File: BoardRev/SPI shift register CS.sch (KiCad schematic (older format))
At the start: 19 parts, among them J1 CONN_06, J10 CONN_07, J2 CONN_06, J3 CONN_06, J4 CONN_06, J5 CONN_06, J6 CONN_06, J7 CONN_06, J8 CONN_06, J9 CONN_07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

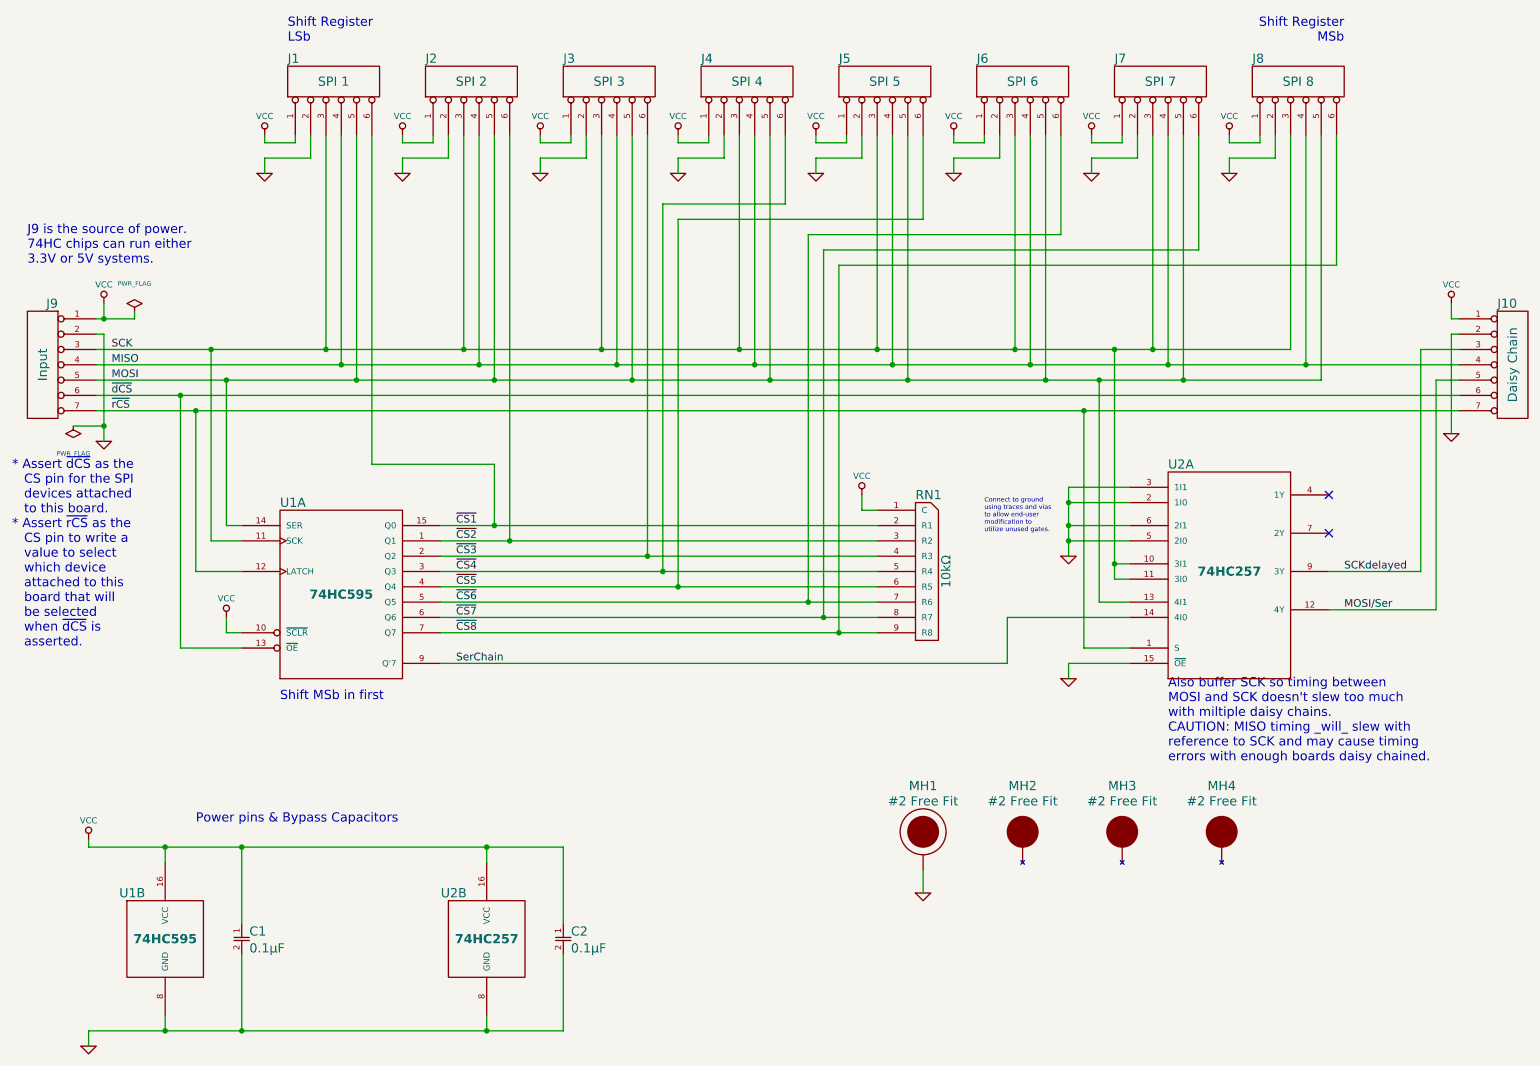
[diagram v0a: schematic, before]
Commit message: Initial 1" square SMT version
Signed-off-by: Chris 'Sembazuru' Elliott <SembazuruCDE@GMail.com>
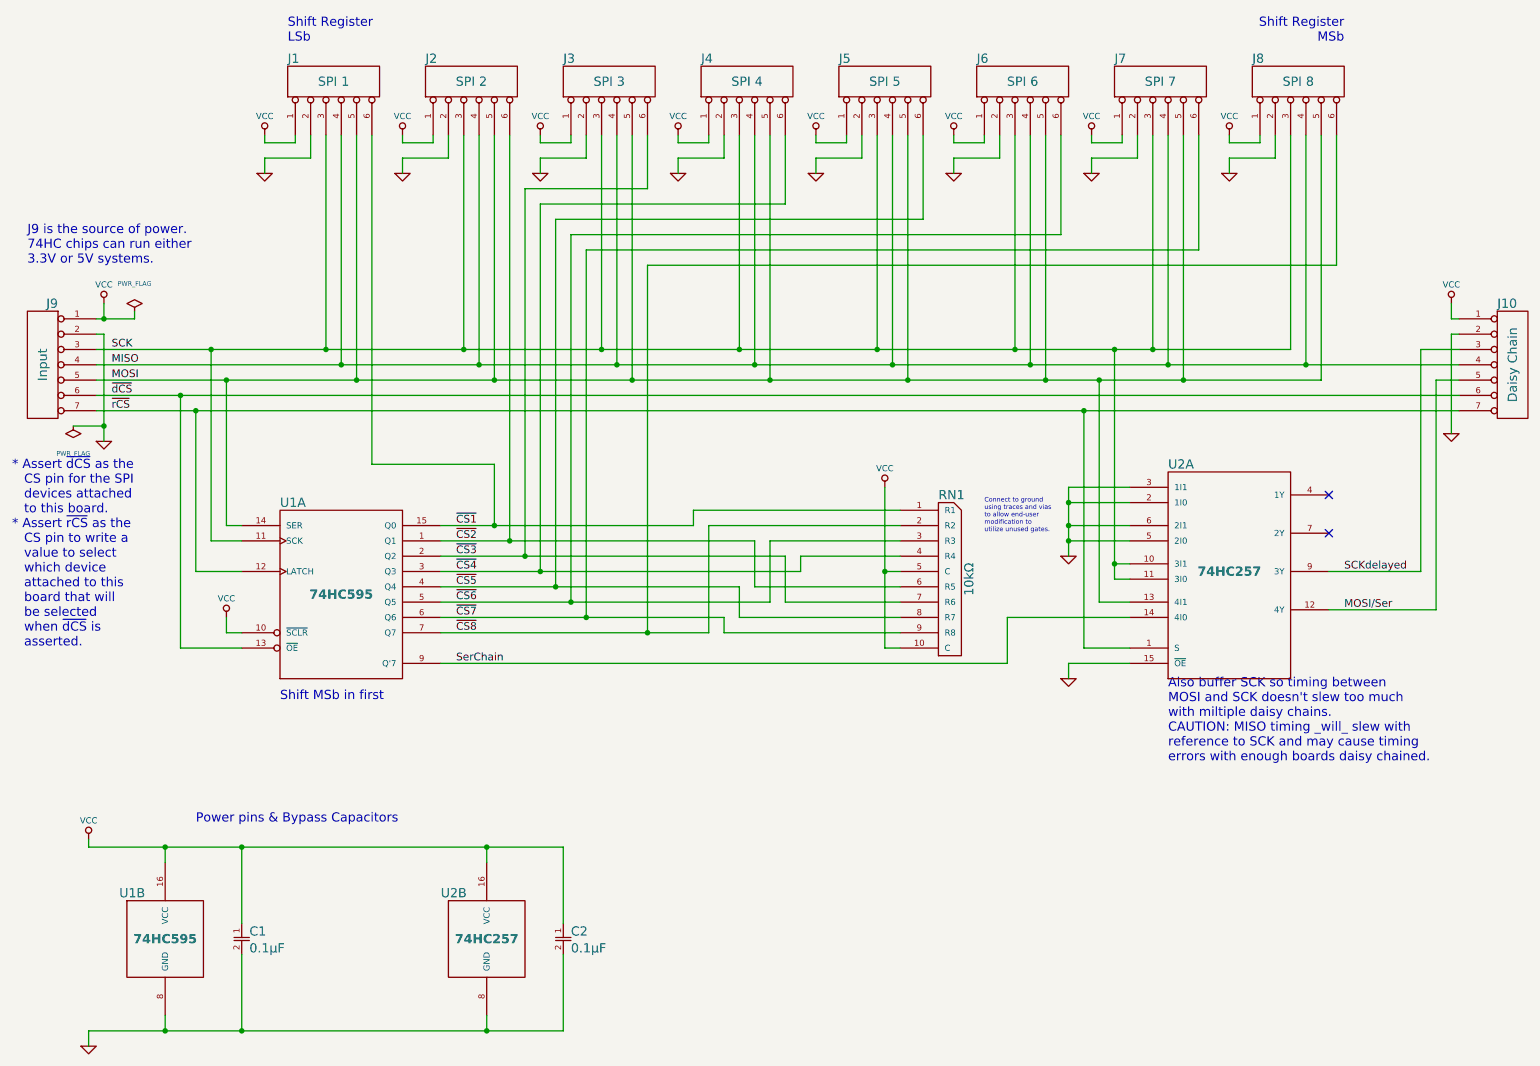
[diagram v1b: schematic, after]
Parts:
- removed MH1: #2 Free Fit, ipc-7251TH Standard:MTGP635H244V8P, symbol MOUNTING_HOLE_PTH
- removed MH2, MH3, MH4: #2 Free Fit, ipc-7251TH Standard:MTGNP635H244Z635P, symbol MOUNTING_HOLE_NPTH
- removed RN1: 10kΩ, ipc-7251TH Standard:SIP249W55P254L2261H495Q9C, symbol RN8BUSSIP
- added RN1: 10kΩ, CDE_misc:RESCAV_EXBA-10N, symbol RN8BUSDIP
- C1, C2: footprint ipc-7251TH Standard:CAPRR254W51L508T318H660P -> AVX-06035C104KAT2A:CAPC1608X90N; CommonPartLibrary (none) -> CPL-CAP-X7R-0603-100NF-50V; Mfg (none) -> AVX; Mfg2 (none) -> Kemet; Mfg2Part (none) -> C0603C104K5RACTU; MfgPart (none) -> 06035C104KAT2A
- J1, J2, J3, J4, J5, J6, J7, J8: footprint ipc-7251TH Standard:HDRV6W64P254_1X6_1524X254X1016P -> ipc-7251TH-standard:HDRV6W64P254_1X6_1524X254X1016P
- U1: footprint ipc-7251TH Standard:DIP762W52P254L2159H381Q16C -> NXP-74HC595PW_118:SOP65P640X110-16N; CommonPartLibrary (none) -> CPL-; Mfg (none) -> Texas Instruments; MfgPart (none) -> SN74HC595PWR
- U2: footprint ipc-7251TH Standard:DIP762W52P254L2159H381Q16C -> TI-SN74HC257PW:SOP65P640X120-16N; CommonPartLibrary (none) -> CPL-; Mfg (none) -> Texas Instruments; MfgPart (none) -> SN74HC257PW
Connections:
- net VCC: now also RN1.10 (C), RN1.5 (C)
- net ~CS1: now also RN1.1 (R1)
- net ~CS2: now also RN1.6 (R5)
- net ~CS3: now also RN1.7 (R6)
- net ~CS4: now also RN1.4 (R4)
- net ~CS5: now also RN1.8 (R7)
- net ~CS6: now also RN1.3 (R3)
- net ~CS7: now also RN1.9 (R8)
- net ~CS8: now also RN1.2 (R2)

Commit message: collected updates
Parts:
- C1, C2: Characteristics (none) -> CAP CER 0.1UF 50V 5% X7R 0603; Critical (none) -> N; Description (none) -> Capacitor - Bypass; MFN (none) -> AVX; MFP (none) -> 06035C104KAT2A; Mfg AVX -> (none); Mfg2 Kemet -> (none); Mfg2Part C0603C104K5RACTU -> (none); MfgPart 06035C104KAT2A -> (none); Notes (none) -> 15WVDC or better, 10% tolerance or better.; Package ID (none) -> 0603 [1608 Metric]; S1PL (none) -> http://www.digikey.com/product-detail/en/06035C104KAT2A/478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; S1PN (none) -> 478-5052-1-ND; S2PL (none) -> http://www.newark.com/avx/06035c104kat2a/ceramic-capacitor-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; S2PN (none) -> 54K2412; Source (none) -> ANY
- J10: Characteristics (none) -> Voltage / Current / Tolerance / Ect specs; CommonPartLibrary (none) -> CPL-; Critical (none) -> Y / N; Description (none) -> Pin header - Daisy chain output to next board.; MFN (none) -> Manufacturer Name; MFP (none) -> Manufacturer Part Number; Notes (none) -> Explain critera for \"ANY\" Source; Package ID (none) -> JEDEC footprint name; S1PL (none) -> Source1 Product Link; S1PN (none) -> Source1 Part Number; S2PL (none) -> Source2 Product Link; S2PN (none) -> Source2 Part Number; Source (none) -> ANY / SPEC
- J9: Characteristics (none) -> Voltage / Current / Tolerance / Ect specs; CommonPartLibrary (none) -> CPL-; Critical (none) -> N; Description (none) -> Pin header - Board input; MFN (none) -> Manufacturer Name; MFP (none) -> Manufacturer Part Number; Notes (none) -> Designed for 0.1\" spacing, 0.25\"sq pins.; Package ID (none) -> JEDEC footprint name; S1PL (none) -> Source1 Product Link; S1PN (none) -> Source1 Part Number; S2PL (none) -> Source2 Product Link; S2PN (none) -> Source2 Part Number; Source (none) -> ANY
- RN1: MFN (none) -> Panasonic; MFP (none) -> EXB-A10P103J; Mfg Panasonic -> (none); MfgPart EXB-A10P103J -> (none)
- U1: MFN (none) -> Texas Instruments; MFP (none) -> SN74HC595PWR; Mfg Texas Instruments -> (none); MfgPart SN74HC595PWR -> (none)
- U2: MFN (none) -> Texas Instruments; MFP (none) -> SN74HC257PW; Mfg Texas Instruments -> (none); MfgPart SN74HC257PW -> (none)
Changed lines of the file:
@@
 Sheet 1 1
 Title "SPI Shift Register 8 Device Select"
-Date "2016-02-25"
-Rev "2.0.0"
+Date "2016-04-16"
+Rev "2.0.1"
 Comp "Sembazuru Circuits"
 Comment1 "Intended to be released as OSHW"
 Comment2 "v1.0 - First iteration"
 Comment3 "v2.0.0 - Convert part numbers and footprints to SMT versions (except for headers)."
-Comment4 ""
+Comment4 "v2.0.1 - Add additional component fields in the spirit of RheingoldHeavy's BOM management"
 $EndDescr
 $Comp
@@
 F 2 "ipc-7251TH Standard:HDRV7W64P254_1X7_1778X254X1016P" H 10300 3150 60  0001 C CNN
 F 3 "" H 10300 3150 60  0000 C CNN
-F 4 "Daisy Chain" V 10300 3150 60  0000 C CNN "Note"
+F 4 "CPL-" H 10300 3150 60  0001 C CNN "CommonPartLibrary"
+F 5 "Manufacturer Name" H 10300 3150 60  0001 C CNN "MFN"
+F 6 "Manufacturer Part Number" H 10300 3150 60  0001 C CNN "MFP"
+F 7 "JEDEC footprint name" H 10300 3150 60  0001 C CNN "Package ID"
+F 8 "Source1 Part Number" H 10300 3150 60  0001 C CNN "S1PN"
+F 9 "Source1 Product Link" H 10300 3150 60  0001 C CNN "S1PL"
+F 10 "Source2 Part Number" H 10300 3150 60  0001 C CNN "S2PN"
+F 11 "Source2 Product Link" H 10300 3150 60  0001 C CNN "S2PL"
+F 12 "Voltage / Current / Tolerance / Ect specs" H 10300 3150 60  0001 C CNN "Characteristics"
+F 13 "Pin header - Daisy chain output to next board." H 10300 3150 60  0001 C CNN "Description"
+F 14 "Y / N" H 10300 3150 60  0001 C CNN "Critical"
+F 15 "ANY / SPEC" H 10300 3150 60  0001 C CNN "Source"
+F 16 "Explain critera for \"ANY\" Source" H 10300 3150 60  0001 C CNN "Notes"
+F 17 "Daisy Chain" V 10300 3150 60  0000 C CNN "Note"
 	1    10300 3150
 	1    0    0    -1
@@
 F 2 "ipc-7251TH Standard:HDRV7W64P254_1X7_1778X254X1016P" H 700 3150 60  0001 C CNN
 F 3 "" H 700 3150 60  0000 C CNN
-F 4 "Input" V 700 3150 60  0000 C CNN "Note"
+F 4 "CPL-" H 700 3150 60  0001 C CNN "CommonPartLibrary"
+F 5 "Manufacturer Name" H 700 3150 60  0001 C CNN "MFN"
+F 6 "Manufacturer Part Number" H 700 3150 60  0001 C CNN "MFP"
+F 7 "JEDEC footprint name" H 700 3150 60  0001 C CNN "Package ID"
+F 8 "Source1 Part Number" H 700 3150 60  0001 C CNN "S1PN"
+F 9 "Source1 Product Link" H 700 3150 60  0001 C CNN "S1PL"
+F 10 "Source2 Part Number" H 700 3150 60  0001 C CNN "S2PN"
+F 11 "Source2 Product Link" H 700 3150 60  0001 C CNN "S2PL"
+F 12 "Voltage / Current / Tolerance / Ect specs" H 700 3150 60  0001 C CNN "Characteristics"
+F 13 "Pin header - Board input" H 700 3150 60  0001 C CNN "Description"
+F 14 "N" H 700 3150 60  0001 C CNN "Critical"
+F 15 "ANY" H 700 3150 60  0001 C CNN "Source"
+F 16 "Designed for 0.1\" spacing, 0.25\"sq pins." H 700 3150 60  0001 C CNN "Notes"
+F 17 "Input" V 700 3150 60  0000 C CNN "Note"
 	1    700  3150
 	-1   0    0    -1
@@
 F 3 "https://octopart.com/sn74hc595pwr-texas+instruments-879136" H 2650 4650 60  0001 C CNN
 F 4 "CPL-" H 2650 4650 60  0001 C CNN "CommonPartLibrary"
-F 5 "Texas Instruments" H 2650 4650 60  0001 C CNN "Mfg"
-F 6 "SN74HC595PWR" H 2650 4650 60  0001 C CNN "MfgPart"
+F 5 "Texas Instruments" H 2650 4650 60  0001 C CNN "MFN"
+F 6 "SN74HC595PWR" H 2650 4650 60  0001 C CNN "MFP"
 	1    2650 4650
 	1    0    0    -1
@@
 F 3 "https://octopart.com/sn74hc257pw-texas+instruments-789437" H 8450 4600 60  0001 C CNN
 F 4 "CPL-" H 8450 4500 60  0001 C CNN "CommonPartLibrary"
-F 5 "Texas Instruments" H 8450 4500 60  0001 C CNN "Mfg"
-F 6 "SN74HC257PW" H 8450 4500 60  0001 C CNN "MfgPart"
+F 5 "Texas Instruments" H 8450 4500 60  0001 C CNN "MFN"
+F 6 "SN74HC257PW" H 8450 4500 60  0001 C CNN "MFP"
 	1    8450 4500
 	1    0    0    -1
@@
 F 3 "https://octopart.com/common-parts-library#CPL-CAP-X7R-0603-100NF-50V" H 2000 6900 60  0001 C CNN
 F 4 "CPL-CAP-X7R-0603-100NF-50V" H 2000 6900 60  0001 C CNN "CommonPartLibrary"
-F 5 "AVX" H 2000 6900 60  0001 C CNN "Mfg"
-F 6 "06035C104KAT2A" H 2000 6900 60  0001 C CNN "MfgPart"
-F 7 "Kemet" H 2000 6900 60  0001 C CNN "Mfg2"
-F 8 "C0603C104K5RACTU" H 2000 6900 60  0001 C CNN "Mfg2Part"
+F 5 "AVX" H 2000 6900 60  0001 C CNN "MFN"
+F 6 "06035C104KAT2A" H 2000 6900 60  0001 C CNN "MFP"
+F 7 "0603 [1608 Metric]" H 2000 6900 60  0001 C CNN "Package ID"
+F 8 "478-5052-1-ND" H 2000 6900 60  0001 C CNN "S1PN"
+F 9 "http://www.digikey.com/product-detail/en/06035C104KAT2A/478-5052-1-ND/" H 2000 6900 60  0001 C CNN "S1PL"
+F 10 "54K2412" H 2000 6900 60  0001 C CNN "S2PN"
+F 11 "http://www.newark.com/avx/06035c104kat2a/ceramic-capacitor-0-1uf-50v-x7r/dp/54K2412" H 2000 6900 60  0001 C CNN "S2PL"
+F 12 "CAP CER 0.1UF 50V 5% X7R 0603" H 2000 6900 60  0001 C CNN "Characteristics"
+F 13 "Capacitor - Bypass" H 2000 6900 60  0001 C CNN "Description"
+F 14 "N" H 2000 6900 60  0001 C CNN "Critical"
+F 15 "ANY" H 2000 6900 60  0001 C CNN "Source"
+F 16 "15WVDC or better, 10% tolerance or better." H 2000 6900 60  0001 C CNN "Notes"
 	1    2000 6900
 	1    0    0    -1
@@
 Connect to ground\nusing traces and vias\nto allow end-user\nmodification to\nutilize unused gates.
 $Comp
-L CAP_NP C2
-U 1 1 56CE7844
-P 4100 6900
-F 0 "C2" H 4150 6950 60  0000 L CNN
-F 1 "0.1µF" H 4150 6840 60  0000 L CNN
-F 2 "AVX-06035C104KAT2A:CAPC1608X90N" H 4100 6900 60  0001 C CNN
-F 3 "https://octopart.com/common-parts-library#CPL-CAP-X7R-0603-100NF-50V" H 4100 6900 60  0001 C CNN
-F 4 "CPL-CAP-X7R-0603-100NF-50V" H 4100 6900 60  0001 C CNN "CommonPartLibrary"
-F 5 "AVX" H 4100 6900 60  0001 C CNN "Mfg"
-F 6 "06035C104KAT2A" H 4100 6900 60  0001 C CNN "MfgPart"
-F 7 "Kemet" H 4100 6900 60  0001 C CNN "Mfg2"
-F 8 "C0603C104K5RACTU" H 4100 6900 60  0001 C CNN "Mfg2Part"
-	1    4100 6900
-	1    0    0    -1
-$EndComp
-$Comp
 L 74HC595 U1
 U 2 1 56CE85CE
@@
 F 3 "https://octopart.com/sn74hc595pwr-texas+instruments-879136" H 1500 6900 60  0001 C CNN
 F 4 "CPL-" H 1500 6900 60  0001 C CNN "CommonPartLibrary"
-F 5 "Texas Instruments" H 1500 6900 60  0001 C CNN "Mfg"
-F 6 "SN74HC595PWR" H 1500 6900 60  0001 C CNN "MfgPart"
+F 5 "Texas Instruments" H 1500 6900 60  0001 C CNN "MFN"
+F 6 "SN74HC595PWR" H 1500 6900 60  0001 C CNN "MFP"
 	2    1500 6900
 	1    0    0    -1
@@
 F 3 "https://octopart.com/sn74hc257pw-texas+instruments-789437" H 3600 7000 60  0001 C CNN
 F 4 "CPL-" H 3600 6900 60  0001 C CNN "CommonPartLibrary"
-F 5 "Texas Instruments" H 3600 6900 60  0001 C CNN "Mfg"
-F 6 "SN74HC257PW" H 3600 6900 60  0001 C CNN "MfgPart"
+F 5 "Texas Instruments" H 3600 6900 60  0001 C CNN "MFN"
+F 6 "SN74HC257PW" H 3600 6900 60  0001 C CNN "MFP"
 	2    3600 6900
 	1    0    0    -1
@@
 F 3 "https://octopart.com/exb-a10p103j-panasonic-42270834" H 6600 4600 60  0001 C CNN
 F 4 "CPL-ARRB-2512-10KOHM-0.062W*" H 6600 4550 30  0001 C CNN "CommonPartLibrary"
-F 5 "Panasonic" H 6600 4550 60  0001 C CNN "Mfg"
-F 6 "EXB-A10P103J" H 6600 4550 60  0001 C CNN "MfgPart"
+F 5 "Panasonic" H 6600 4550 60  0001 C CNN "MFN"
+F 6 "EXB-A10P103J" H 6600 4550 60  0001 C CNN "MFP"
 	1    6600 4550
 	1    0    0    -1
@@
 	5350 4600 6300 4600
 Connection ~ 3750 4300
+$Comp
+L CAP_NP C2
+U 1 1 5711DF92
+P 4100 6900
+F 0 "C2" H 4150 6950 60  0000 L CNN
+F 1 "0.1µF" H 4150 6840 60  0000 L CNN
+F 2 "AVX-06035C104KAT2A:CAPC1608X90N" H 4100 6900 60  0001 C CNN
+F 3 "https://octopart.com/common-parts-library#CPL-CAP-X7R-0603-100NF-50V" H 4100 6900 60  0001 C CNN
+F 4 "CPL-CAP-X7R-0603-100NF-50V" H 4100 6900 60  0001 C CNN "CommonPartLibrary"
+F 5 "AVX" H 4100 6900 60  0001 C CNN "MFN"
+F 6 "06035C104KAT2A" H 4100 6900 60  0001 C CNN "MFP"
+F 7 "0603 [1608 Metric]" H 4100 6900 60  0001 C CNN "Package ID"
+F 8 "478-5052-1-ND" H 4100 6900 60  0001 C CNN "S1PN"
+F 9 "http://www.digikey.com/product-detail/en/06035C104KAT2A/478-5052-1-ND/" H 4100 6900 60  0001 C CNN "S1PL"
+F 10 "54K2412" H 4100 6900 60  0001 C CNN "S2PN"
+F 11 "http://www.newark.com/avx/06035c104kat2a/ceramic-capacitor-0-1uf-50v-x7r/dp/54K2412" H 4100 6900 60  0001 C CNN "S2PL"
+F 12 "CAP CER 0.1UF 50V 5% X7R 0603" H 4100 6900 60  0001 C CNN "Characteristics"
+F 13 "Capacitor - Bypass" H 4100 6900 60  0001 C CNN "Description"
+F 14 "N" H 4100 6900 60  0001 C CNN "Critical"
+F 15 "ANY" H 4100 6900 60  0001 C CNN "Source"
+F 16 "15WVDC or better, 10% tolerance or better." H 4100 6900 60  0001 C CNN "Notes"
+	1    4100 6900
+	1    0    0    -1
+$EndComp
 $EndSCHEMATC
